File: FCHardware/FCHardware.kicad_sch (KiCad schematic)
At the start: 43 parts, among them J2 USB_C_Receptacle_USB2.0_16P, SW1 SW_Push, U1 ESC_Xrotor_65A_4in1, U2 ESP32-S3-MINI-1U, U3 TPSM63603, U4 USBLC6-2SC6, U5 MPU-6050

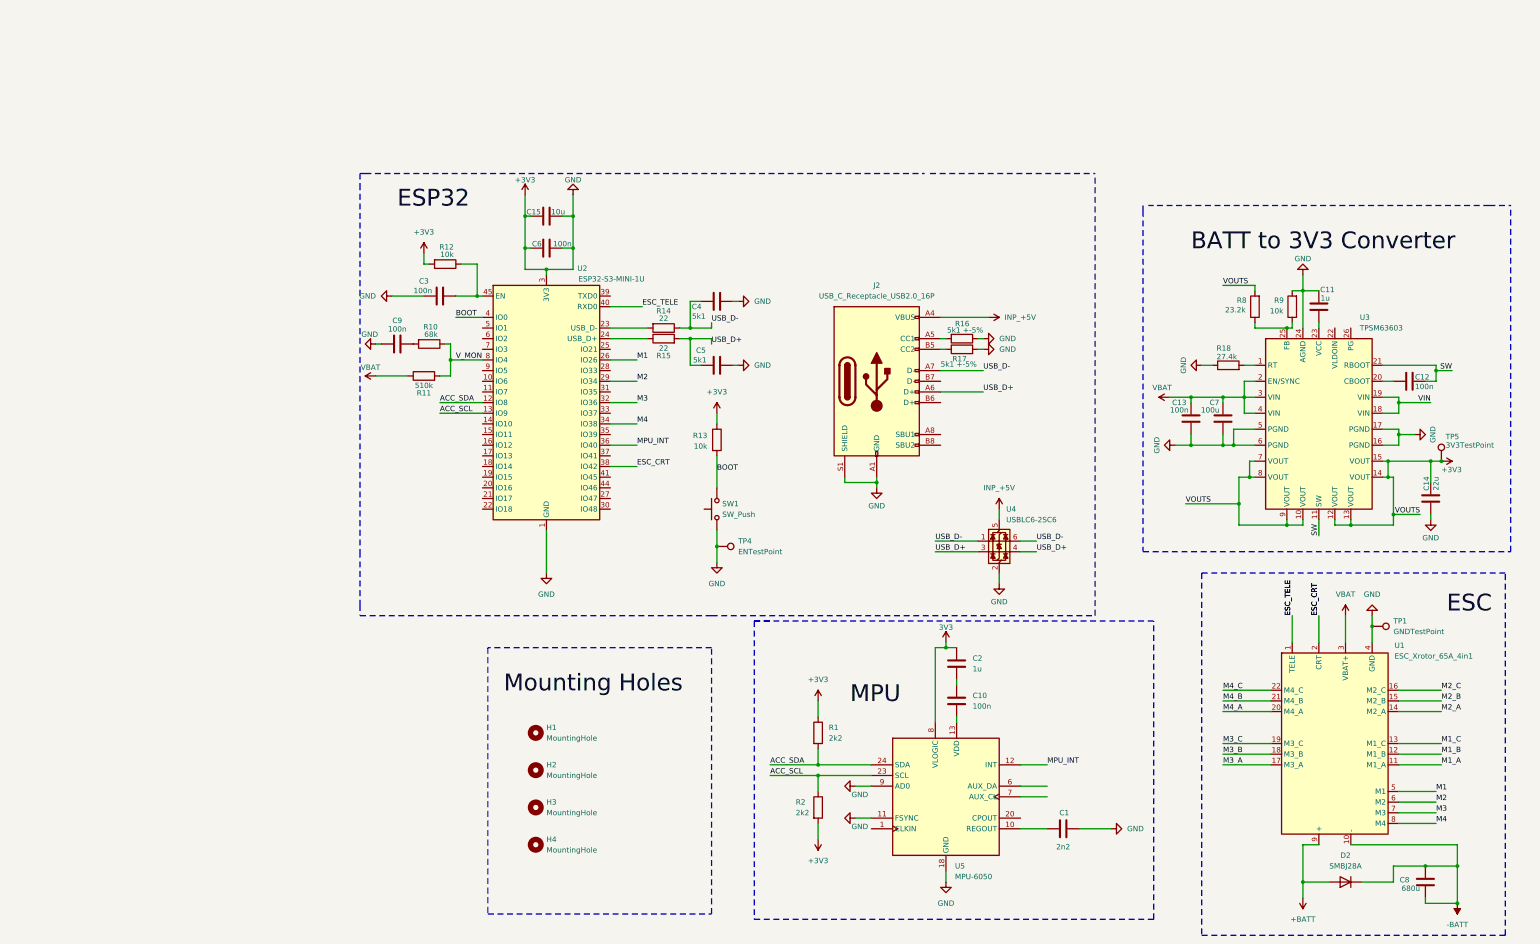
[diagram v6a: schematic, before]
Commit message: Passed ERC, fixed shorts
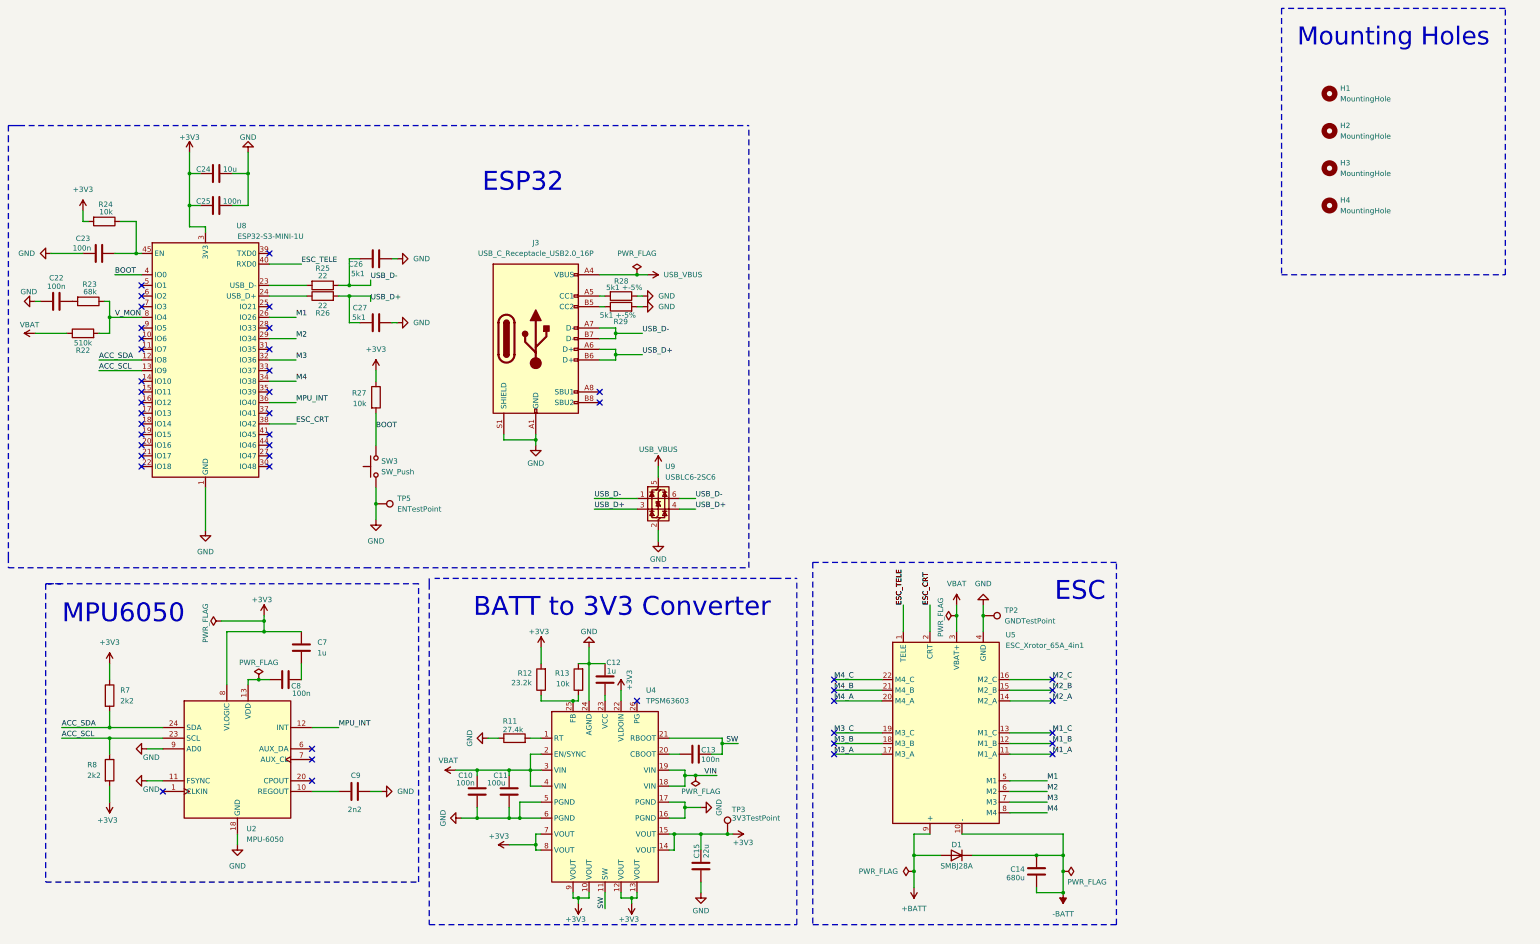
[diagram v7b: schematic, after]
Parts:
- removed C15: 10u, symbol Device:C
- removed C3, C6, C9: 100n, symbol Device:C
- removed C4, C5: 5k1, symbol Device:C
- removed J2: USB_C_Receptacle_USB2.0_16P, symbol Connector:USB_C_Receptacle_USB2.0_16P
- removed R10: 68k, symbol Device:R
- removed R11: 510k, symbol Device:R
- removed R12, R13: 10k, symbol Device:R
- removed R14, R15: 22, symbol Device:R
- removed R16, R17: 5k1 +-5%, symbol Device:R
- removed SW1: SW_Push, symbol Switch:SW_Push
- removed TP4: ENTestPoint, symbol Connector:TestPoint
- removed U2: ESP32-S3-MINI-1U, RF_Module:ESP32-S2-MINI-1U, symbol RF_Module:ESP32-S3-MINI-1U
- removed U4: USBLC6-2SC6, Package_TO_SOT_SMD:SOT-23-6, symbol Power_Protection:USBLC6-2SC6
- added C22, C23, C25: 100n, symbol Device:C
- added C24: 10u, symbol Device:C
- added C26, C27: 5k1, symbol Device:C
- added J3: USB_C_Receptacle_USB2.0_16P, symbol Connector:USB_C_Receptacle_USB2.0_16P
- added R22: 510k, symbol Device:R
- added R23: 68k, symbol Device:R
- added R24, R27: 10k, symbol Device:R
- added R25, R26: 22, symbol Device:R
- added R28, R29: 5k1 +-5%, symbol Device:R
- added SW3: SW_Push, symbol Switch:SW_Push
- added TP5: ENTestPoint, symbol Connector:TestPoint
- added U8: ESP32-S3-MINI-1U, RF_Module:ESP32-S2-MINI-1U, symbol RF_Module:ESP32-S3-MINI-1U
- added U9: USBLC6-2SC6, Package_TO_SOT_SMD:SOT-23-6, symbol Power_Protection:USBLC6-2SC6
- renumbered C13 to C10, C7 to C11, C11 to C12, C12 to C13, C8 to C14, C14 to C15, C2 to C7, C10 to C8, C1 to C9, D2 to D1, R18 to R11, R8 to R12, R9 to R13, R1 to R7, R2 to R8, TP1 to TP2, TP5 to TP3, U5 to U2, U3 to U4, U1 to U5
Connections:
- net 3V3 is gone; now on net +3V3: C7.2, U2.8 (VLOGIC)
- net +3V3: now also U4.22 (VLDOIN), C24.2, C25.2, R24.2, R27.1, U8.3 (3V3); no longer C10.2, C11.2, C12.1, C15.2, C9.2, R11.1, R13.2, TP2.1, U2.11 (FSYNC), U2.18 (GND), U2.9 (AD0), U4.16 (PGND), U4.17 (PGND), U4.24 (AGND), U4.5 (PGND), U4.6 (PGND), U5.4 (GND)
- net ACC_SCL: now also U8.13 (IO9)
- net ACC_SDA: now also U8.12 (IO8)
- net BOOT: now also R27.2, SW3.2, U8.4 (IO0)
- net ESC_CRT: now also U8.38 (IO42)
- net ESC_TELE: now also U8.40 (RXD0)
- net M1: now also U8.26 (IO26)
- net M2: now also U8.29 (IO34)
- net M3: now also U8.32 (IO36)
- net M4: now also U8.34 (IO38)
- net MPU_INT: now also U8.36 (IO40)
- net USB_D+: now also C27.1, J3.A6 (D+), J3.B6 (D+), R26.2, U9.3 (I/O2), U9.4 (I/O2)
- net USB_D-: now also C26.1, J3.A7 (D-), J3.B7 (D-), R25.1, U9.1 (I/O1), U9.6 (I/O1)
- net VBAT: now also R22.1
- net V_MON: now also R22.2, R23.1, U8.8 (IO4)
- net at C8.1: now also C7.1; no longer U2.13 (VDD)
- net at C8.2: now also U2.13 (VDD); no longer C7.1
- new net: C23.2, R24.1, U8.45 (EN)
- new net: J3.B5 (CC2), R29.1
- new net: J3.A5 (CC1), R28.2
- new net: R25.2, U8.23 (USB_D-)
- new net: R26.1, U8.24 (USB_D+)
- new net: C22.2, R23.2
- new net GND: C10.2, C11.2, C12.1, C15.2, C22.1, C23.1, C24.1, C25.1, C26.2, C27.2, C9.2, J3.A1 (GND), J3.A12 (GND), J3.B1 (GND), J3.B12 (GND), J3.S1 (SHIELD), R11.1, R13.2, R28.1, R29.2, SW3.1, TP2.1, TP5.1, U2.11 (FSYNC), U2.18 (GND), U2.9 (AD0), U4.16 (PGND), U4.17 (PGND), U4.24 (AGND), U4.5 (PGND), U4.6 (PGND), U5.4 (GND), U8.1 (GND), U8.2 (GND), U8.42 (GND), U8.43 (GND), U8.46 (GND), U8.47 (GND), U8.48 (GND), U8.49 (GND), U8.50 (GND), U8.51 (GND), U8.52 (GND), U8.53 (GND), U8.54 (GND), U8.55 (GND), U8.56 (GND), U8.57 (GND), U8.58 (GND), U8.59 (GND), U8.60 (GND), U8.61 (GND), U8.62 (GND), U8.63 (GND), U8.64 (GND), U8.65 (GND), U9.2 (GND)
- new net USB_VBUS: J3.A4 (VBUS), J3.A9 (VBUS), J3.B4 (VBUS), J3.B9 (VBUS), U9.5 (VBUS)
- no-connect marks 0 -> 45
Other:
- note added: "BATT to 3V3 Converter"
- note added: "ESC"
- note added: "ESP32"
- note added: "MPU6050"
- note added: "Mounting Holes"
- moved on the sheet: C10, C11, C12, C13, C14, C15, C7, C8, C9, D1, H1, H2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

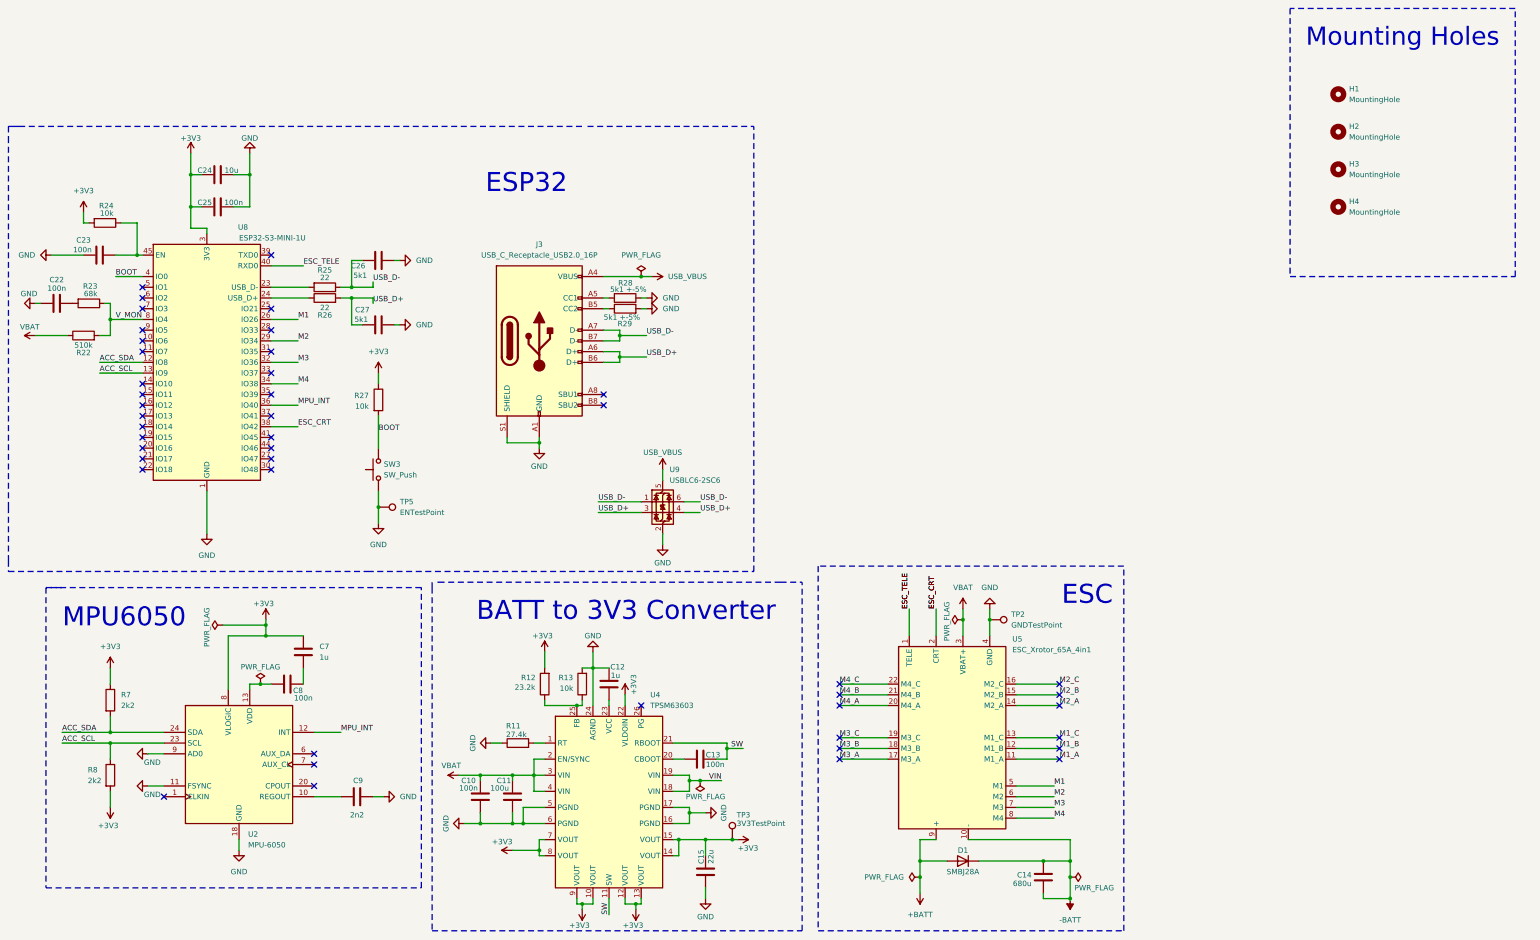
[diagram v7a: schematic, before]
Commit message: Assigned all the footprints
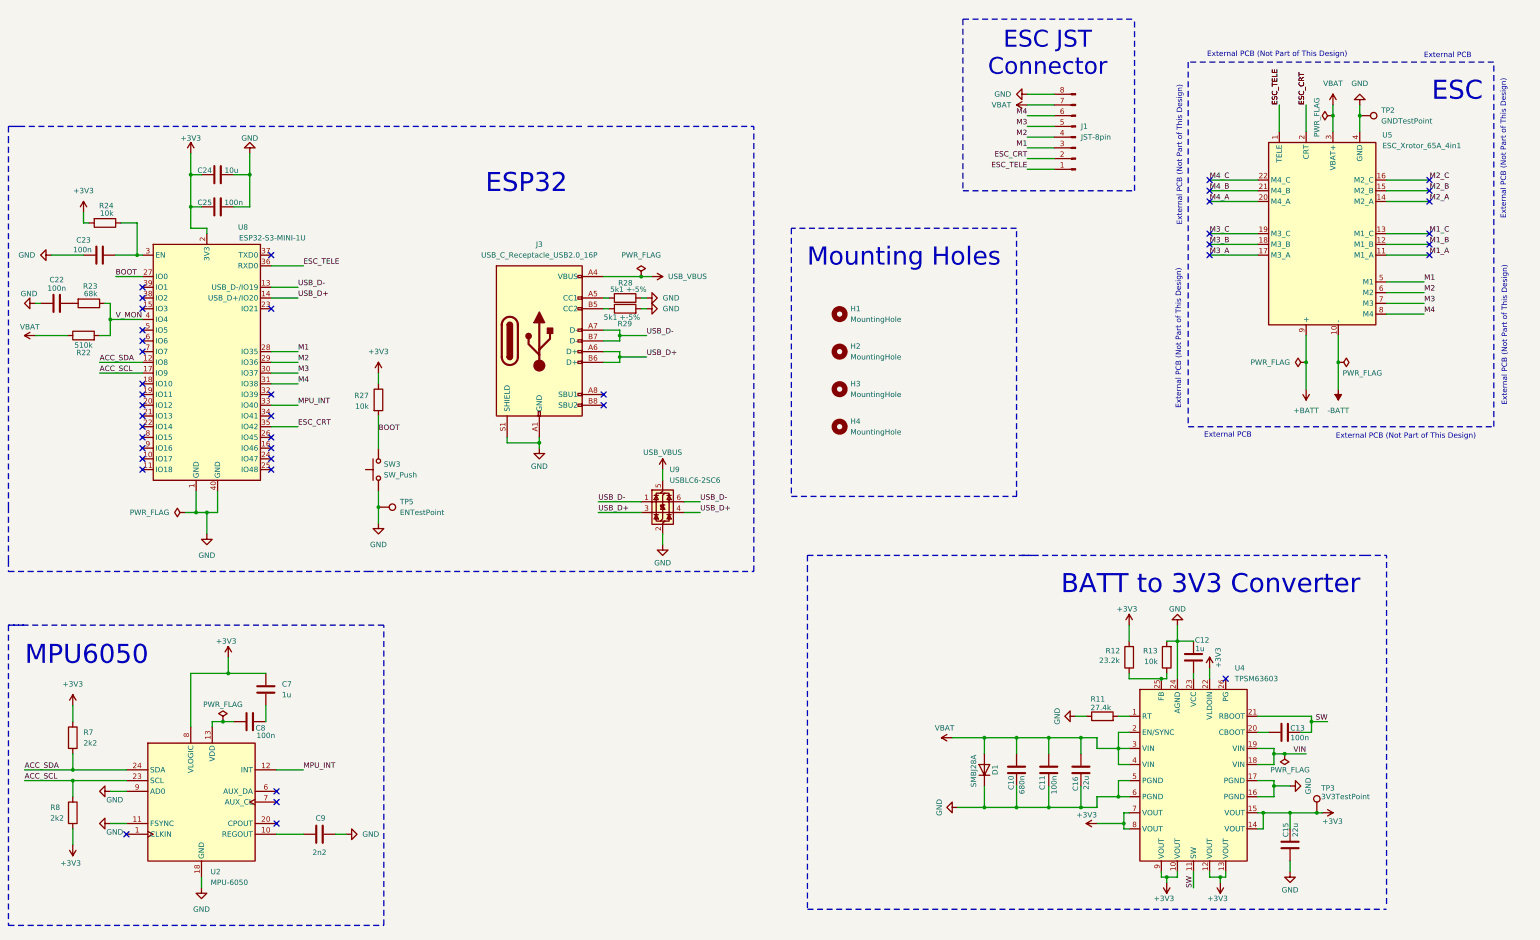
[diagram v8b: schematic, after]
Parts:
- removed C14: 680u, symbol Device:C
- removed C26, C27: 5k1, symbol Device:C
- removed R25, R26: 22, symbol Device:R
- added C16: 22u, Capacitor_SMD:C_1206_3216Metric_Pad1.33x1.80mm_HandSolder, symbol Device:C
- added J1: JST-8pin, Connector_JST:JST_GH_SM08B-GHS-TB_1x08-1MP_P1.25mm_Horizontal, symbol Connector:Conn_01x08_Pin
- C10: value 100n -> 680n; footprint (none) -> Capacitor_SMD:C_1210_3225Metric_Pad1.33x2.70mm_HandSolder
- C11: value 100u -> 100n; footprint (none) -> Capacitor_SMD:C_0603_1608Metric_Pad1.08x0.95mm_HandSolder
- C12, C13, C22, C23, C25, C7, C8, C9: footprint (none) -> Capacitor_SMD:C_0603_1608Metric_Pad1.08x0.95mm_HandSolder
- C15: footprint (none) -> Capacitor_SMD:C_1206_3216Metric_Pad1.33x1.80mm_HandSolder
- C24: footprint (none) -> Capacitor_SMD:C_0805_2012Metric_Pad1.18x1.45mm_HandSolder
- D1: footprint (none) -> Diode_SMD:D_SMB_Handsoldering
- H1, H2, H3, H4: footprint (none) -> MountingHole:MountingHole_3.2mm_M3
- J3: footprint (none) -> Connector_USB:USB_C_Receptacle_GCT_USB4105-xx-A_16P_TopMnt_Horizontal
- R11, R12, R13, R22, R23, R24, R27, R28, R29, R7, R8: footprint (none) -> Resistor_SMD:R_0603_1608Metric_Pad0.98x0.95mm_HandSolder
- SW3: footprint (none) -> Button_Switch_THT:SW_PUSH_6mm
- TP2, TP3, TP5: footprint (none) -> TestPoint:TestPoint_Pad_D1.5mm
- U4: footprint RF_Module:ESP32-C3-WROOM-02 -> FCFootprints:CONV_TPSM63603EXTRDHR
- U5: footprint - -> (none)
- U8: footprint RF_Module:ESP32-S2-MINI-1U -> RF_Module:ESP32-S3-WROOM-1U; symbol RF_Module:ESP32-S3-MINI-1U -> Custom_ESP32_Library:ESP32-S3-MINI-1U
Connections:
- net +3V3: now also U8.2 (3V3); no longer U8.3 (3V3)
- net +BATT: no longer D1.2 (A)
- net -BATT: no longer D1.1 (K)
- net ACC_SCL: now also U8.17 (IO9); no longer U8.13 (IO9)
- net BOOT: now also U8.27 (IO0); no longer U8.4 (IO0)
- net ESC_CRT: now also U8.35 (IO42), J1.2 (Pin_2); no longer U8.38 (IO42)
- net ESC_TELE: now also U8.36 (RXD0), J1.1 (Pin_1); no longer U8.40 (RXD0)
- net GND: now also C10.1, C11.1, D1.1 (K), U8.40 (GND), C16.1, J1.8 (Pin_8); no longer C10.2, C11.2, U8.2 (GND), U8.42 (GND), U8.43 (GND), U8.46 (GND), U8.47 (GND), U8.48 (GND), U8.49 (GND), U8.50 (GND), U8.51 (GND), U8.52 (GND), U8.53 (GND), U8.54 (GND), U8.55 (GND), U8.56 (GND), U8.57 (GND), U8.58 (GND), U8.59 (GND), U8.60 (GND), U8.61 (GND), U8.62 (GND), U8.63 (GND), U8.64 (GND), U8.65 (GND)
- net M1: now also U8.28 (IO35), J1.3 (Pin_3); no longer U8.26 (IO26)
- net M2: now also J1.4 (Pin_4)
- net M3: now also U8.30 (IO37), J1.5 (Pin_5); no longer U8.32 (IO36)
- net M4: now also U8.31 (IO38), J1.6 (Pin_6); no longer U8.34 (IO38)
- net MPU_INT: now also U8.33 (IO40); no longer U8.36 (IO40)
- net USB_D+: now also U8.14 (USB_D+/IO20)
- net USB_D-: now also U8.13 (USB_D-/IO19)
- net VBAT: now also C10.2, C11.2, D1.2 (A), C16.2, J1.7 (Pin_7); no longer C10.1, C11.1
- net V_MON: now also U8.4 (IO4); no longer U8.8 (IO4)
- net at C23.2, R24.1: now also U8.3 (EN); no longer U8.45 (EN)
- no-connect marks 45 -> 42
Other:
- note added: "ESC JST Connector"
- note added: "External PCB"
- note added: "External PCB (Not Part of This Design)"
- moved on the sheet: C10, C11, C12, C13, C15, C7, C8, C9, D1, H1, H2, H3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
